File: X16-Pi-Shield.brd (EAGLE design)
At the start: 80.2 x 73 mm, 55 parts, among them J1 CONN_DF13-4P-1.25DSA, J2 CONN_DF13-4P-1.25DSA, J3 CONN_DF13-4P-1.25DSA, Q2 2.5A/30V/105mΩ, Q3 220mA/50V/3.5Ω, Q4 220mA/50V/3.5Ω, Q5 220mA/50V/3.5Ω, U2 MAX1136EUA-T, Y2 ECS-80-S-4X

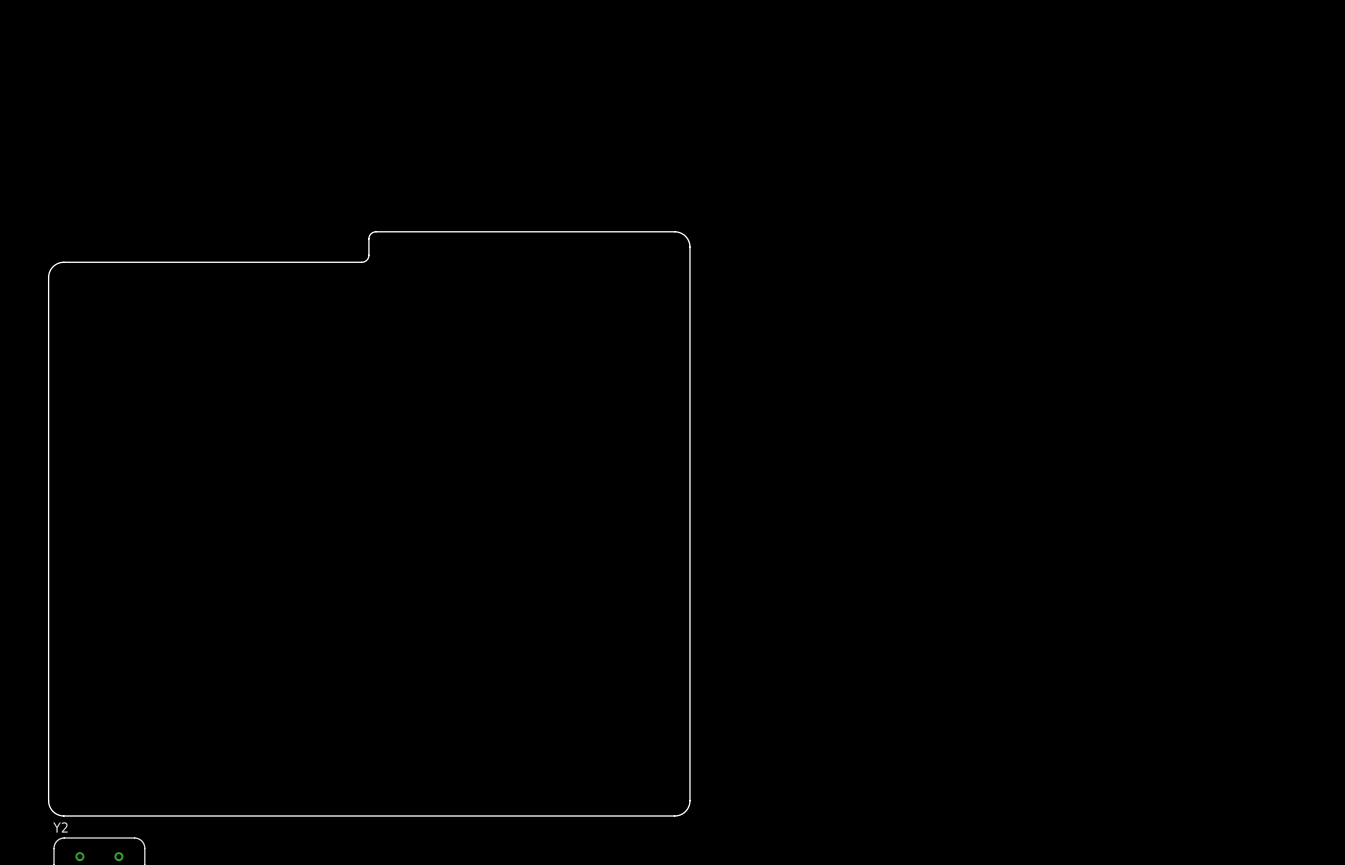
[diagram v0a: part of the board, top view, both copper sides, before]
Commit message: edited schematic for new connector
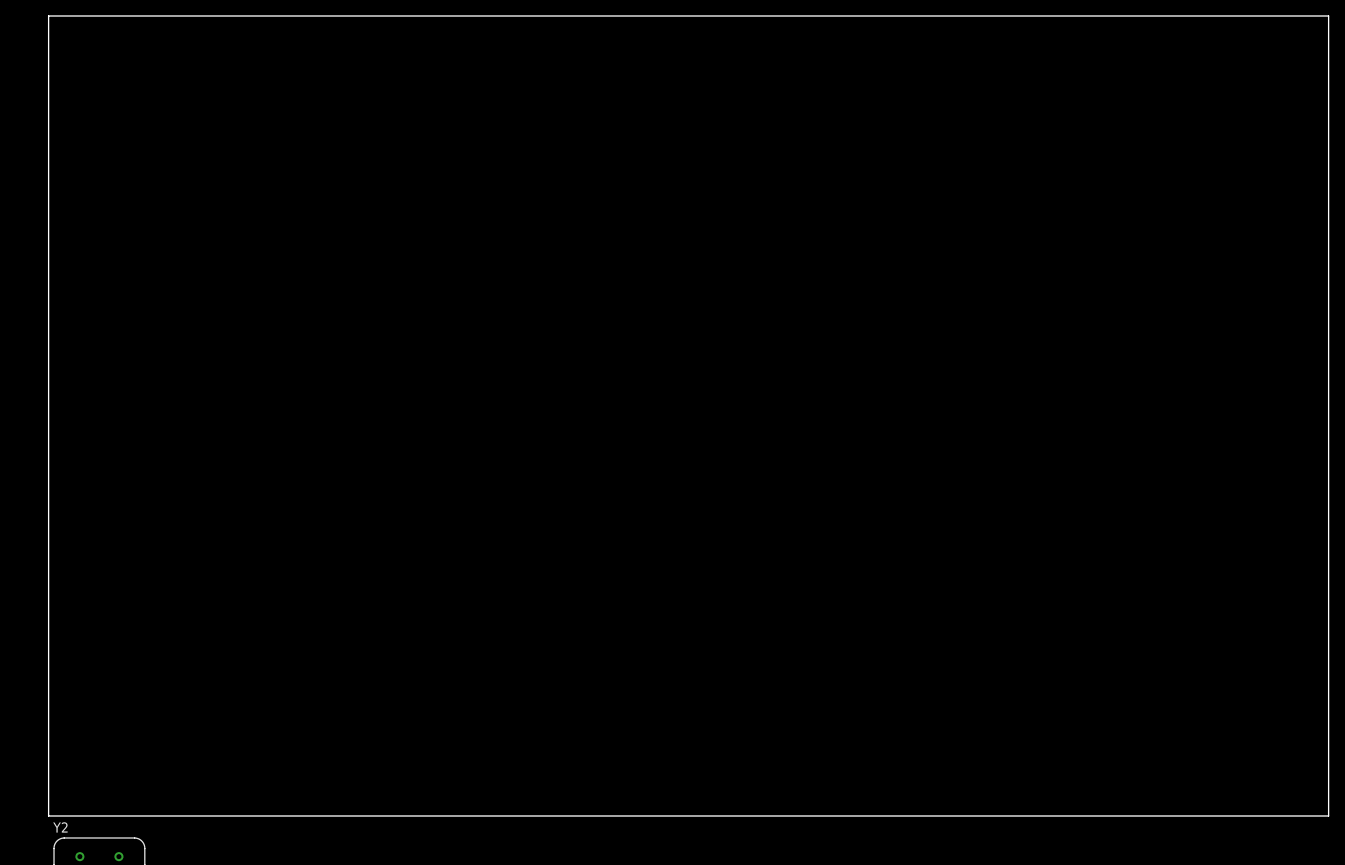
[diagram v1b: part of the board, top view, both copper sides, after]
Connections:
- net GPIO_6 renamed SA0
- removed net N$42: U$1.1
- new net CTRL: U$1.15
- new net DGND: U$1.31
- new net SA1: U$1.12
- new net SALERT: U$1.33
- net 3V3: now also U$1.1
- net GPIO_10: no longer U$1.31
- net GPIO_11: no longer U$1.15
- net GPIO_7: no longer U$1.12
- net GPIO_8: no longer U$1.32
- net GPIO_9: no longer U$1.33
- net SCL: now also U$1.32
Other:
- board size 80.2 x 73 mm -> 160 x 100 mm

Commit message: added connector
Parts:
- added J4: SAMTEC-HTST-110-04-X-D-RAJ, SAMTEC-HTST-110-04-X-D-RA:SAMTEC-HTST-110-04-X-D-RA
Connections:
- net 5V: now also J4.1
- net CLK: now also J4.18
- net CS: now also J4.20
- net CTRL: now also J4.7
- net DGND: now also J4.9
- net GND: now also J4.3
- net GPIO1: now also J4.2
- net GPIO2: now also J4.4
- net GPIO3: now also J4.6
- net GPIO4: now also J4.8
- net MISO: now also J4.14
- net MOSI: now also J4.16
- net SA0: now also J4.19
- net SA1: now also J4.17
- net SALERT: now also J4.13
- net SCL: now also J4.15
- net SDA: now also J4.11
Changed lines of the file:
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@@
 <attribute name="SPICEPREFIX" value="X" x="-24.13" y="-312.42" size="1.778" layer="27" display="off"/>
+</element>
+<element name="J4" library="SAMTEC-HTST-110-04-X-D-RA" package="SAMTEC-HTST-110-04-X-D-RA" value="SAMTEC-HTST-110-04-X-D-RAJ" x="-5.08" y="-325.12" smashed="yes">
+<attribute name="NAME" x="13.123" y="-316.266" size="1.905" layer="25"/>
+<attribute name="VALUE" x="-5.08" y="-319.216" size="0.635" layer="27" align="bottom-center"/>
 </element>
 </elements>
@@
 <contactref element="U$9" pad="6"/>
 <contactref element="U$9" pad="10"/>
+<contactref element="J4" pad="3"/>
 <wire x1="-22.01" y1="-234.95" x2="-18.2" y2="-234.95" width="0" layer="19" extent="1-1"/>
 <wire x1="-22.86" y1="-240.03" x2="-22.01" y2="-234.95" width="0" layer="19" extent="1-1"/>
@@
 <wire x1="-11.938" y1="-311.15" x2="-11.85" y2="-294.64" width="0" layer="19" extent="1-1"/>
 <wire x1="-17.018" y1="-311.15" x2="-11.938" y2="-311.15" width="0" layer="19" extent="1-1"/>
+<wire x1="3.81" y1="-317.246" x2="-11.938" y2="-311.15" width="0" layer="19" extent="1-1"/>
 <wire x1="-22.01" y1="-182.88" x2="-24.13" y2="-204.47" width="0" layer="19" extent="1-1"/>
 <wire x1="-12.065" y1="-177.8" x2="-22.01" y2="-182.88" width="0" layer="19" extent="1-1"/>
@@
 <contactref element="U$1" pad="24"/>
 <contactref element="J12" pad="5"/>
+<contactref element="J4" pad="20"/>
 <wire x1="21.0566" y1="-19.8882" x2="-12.7" y2="-96.52" width="0" layer="19" extent="1-1"/>
+<wire x1="-16.51" y1="-319.786" x2="-12.7" y2="-96.52" width="0" layer="19" extent="1-1"/>
 </signal>
 <signal name="A_INT">
@@
 <contactref element="U$1" pad="23"/>
 <contactref element="J12" pad="2"/>
+<contactref element="J4" pad="18"/>
 <wire x1="21.0566" y1="-22.4282" x2="-20.32" y2="-96.52" width="0" layer="19" extent="1-1"/>
+<wire x1="-13.97" y1="-319.786" x2="-20.32" y2="-96.52" width="0" layer="19" extent="1-1"/>
 </signal>
 <signal name="MISO">
 <contactref element="U$1" pad="21"/>
 <contactref element="J12" pad="4"/>
+<contactref element="J4" pad="14"/>
 <wire x1="18.5166" y1="-22.4282" x2="-15.24" y2="-96.52" width="0" layer="19" extent="1-1"/>
+<wire x1="-8.89" y1="-319.786" x2="-15.24" y2="-96.52" width="0" layer="19" extent="1-1"/>
 </signal>
 <signal name="MOSI">
 <contactref element="U$1" pad="19"/>
 <contactref element="J12" pad="3"/>
+<contactref element="J4" pad="16"/>
 <wire x1="15.9766" y1="-22.4282" x2="-17.78" y2="-96.52" width="0" layer="19" extent="1-1"/>
+<wire x1="-11.43" y1="-319.786" x2="-17.78" y2="-96.52" width="0" layer="19" extent="1-1"/>
 </signal>
 <signal name="N$34">
@@
 <contactref element="J3" pad="3"/>
 <contactref element="J2" pad="3"/>
+<contactref element="J4" pad="11"/>
 <wire x1="-17.78" y1="-116.84" x2="-9.525" y2="-177.8" width="0" layer="19" extent="1-1"/>
 <wire x1="-23.71" y1="-107.95" x2="-17.78" y2="-116.84" width="0" layer="19" extent="1-1"/>
@@
 <wire x1="-15.56" y1="-289.29" x2="-9.525" y2="-177.8" width="0" layer="19" extent="1-1"/>
 <wire x1="-14.39" y1="-299.72" x2="-15.56" y2="-289.29" width="0" layer="19" extent="1-1"/>
+<wire x1="-6.35" y1="-317.246" x2="-14.39" y2="-299.72" width="0" layer="19" extent="1-1"/>
 </signal>
 <signal name="3V3">
@@
 <contactref element="R24" pad="2"/>
 <contactref element="U$1" pad="32"/>
+<contactref element="J4" pad="15"/>
 <wire x1="-20.32" y1="-116.84" x2="-6.985" y2="-177.8" width="0" layer="19" extent="1-1"/>
 <wire x1="-23.71" y1="-111.76" x2="-20.32" y2="-116.84" width="0" layer="19" extent="1-1"/>
@@
 <wire x1="-20.64" y1="-289.29" x2="-6.985" y2="-177.8" width="0" layer="19" extent="1-1"/>
 <wire x1="-18.2" y1="-299.72" x2="-20.64" y2="-289.29" width="0" layer="19" extent="1-1"/>
+<wire x1="-11.43" y1="-317.246" x2="-18.2" y2="-299.72" width="0" layer="19" extent="1-1"/>
 </signal>
 <signal name="PI_POWER">
@@
 <contactref element="C13" pad="1"/>
 <contactref element="U$9" pad="8"/>
+<contactref element="J4" pad="1"/>
 <wire x1="-23.65" y1="-227.965" x2="-23.65" y2="-229.235" width="0" layer="19" extent="1-1"/>
 <wire x1="-23.65" y1="-226.695" x2="-23.65" y2="-227.965" width="0" layer="19" extent="1-1"/>
@@
 <wire x1="-22.01" y1="-303.53" x2="-22.01" y2="-299.72" width="0" layer="19" extent="1-1"/>
 <wire x1="-14.478" y1="-311.15" x2="-22.01" y2="-303.53" width="0" layer="19" extent="1-1"/>
+<wire x1="6.35" y1="-317.246" x2="-14.478" y2="-311.15" width="0" layer="19" extent="1-1"/>
 </signal>
 <signal name="IMU_RESET1">
@@
 <signal name="GPIO1">
 <contactref element="U$9" pad="1"/>
+<contactref element="J4" pad="2"/>
+<wire x1="6.35" y1="-319.786" x2="-22.098" y2="-308.61" width="0" layer="19" extent="1-1"/>
 </signal>
 <signal name="GPIO2">
 <contactref element="U$9" pad="3"/>
+<contactref element="J4" pad="4"/>
+<wire x1="3.81" y1="-319.786" x2="-19.558" y2="-308.61" width="0" layer="19" extent="1-1"/>
 </signal>
 <signal name="GPIO3">
 <contactref element="U$9" pad="5"/>
+<contactref element="J4" pad="6"/>
+<wire x1="1.27" y1="-319.786" x2="-17.018" y2="-308.61" width="0" layer="19" extent="1-1"/>
 </signal>
 <signal name="GPIO4">
 <contactref element="U$9" pad="7"/>
+<contactref element="J4" pad="8"/>
+<wire x1="-1.27" y1="-319.786" x2="-14.478" y2="-308.61" width="0" layer="19" extent="1-1"/>
 </signal>
 <signal name="GPIO5">
@@
 <signal name="CTRL">
 <contactref element="U$1" pad="15"/>
+<contactref element="J4" pad="7"/>
+<wire x1="10.8966" y1="-22.4282" x2="-1.27" y2="-317.246" width="0" layer="19" extent="1-1"/>
 </signal>
 <signal name="DGND">
 <contactref element="U$1" pad="31"/>
+<contactref element="J4" pad="9"/>
+<wire x1="31.2166" y1="-22.4282" x2="-3.81" y2="-317.246" width="0" layer="19" extent="1-1"/>
 </signal>
 <signal name="SALERT">
 <contactref element="U$1" pad="33"/>
+<contactref element="J4" pad="13"/>
+<wire x1="33.7566" y1="-22.4282" x2="-8.89" y2="-317.246" width="0" layer="19" extent="1-1"/>
 </signal>
 <signal name="SA1">
 <contactref element="U$1" pad="12"/>
+<contactref element="J4" pad="17"/>
+<wire x1="5.8166" y1="-19.8882" x2="-13.97" y2="-317.246" width="0" layer="19" extent="1-1"/>
 </signal>
 <signal name="SA0">
 <contactref element="U$1" pad="40"/>
+<contactref element="J4" pad="19"/>
+<wire x1="41.3766" y1="-19.8882" x2="-16.51" y2="-317.246" width="0" layer="19" extent="1-1"/>
 </signal>
 </signals>

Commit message: added some nets
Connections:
- removed net N$34: U$1.17
- net 3V3: now also U$1.17
- net GPIO5: now also J4.10
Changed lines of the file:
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@@
 <wire x1="-11.43" y1="-319.786" x2="-17.78" y2="-96.52" width="0" layer="19" extent="1-1"/>
-</signal>
-<signal name="N$34">
-<contactref element="U$1" pad="17"/>
 </signal>
 <signal name="GPIO_11">
@@
 <contactref element="U$9" pad="12"/>
 <contactref element="U$1" pad="1"/>
+<contactref element="U$1" pad="17"/>
 <wire x1="-24.13" y1="-199.39" x2="-18.2" y2="-212.09" width="0" layer="19" extent="1-1"/>
 <wire x1="-19.4564" y1="-196.85" x2="-24.13" y2="-199.39" width="0" layer="19" extent="1-1"/>
@@
 <wire x1="-19.715" y1="-71.12" x2="-19.715" y2="-80.01" width="0" layer="19" extent="1-1"/>
 <wire x1="-6.87" y1="-22.43" x2="-19.715" y2="-71.12" width="0" layer="19" extent="1-1"/>
+<wire x1="13.4366" y1="-22.4282" x2="-6.87" y2="-22.43" width="0" layer="19" extent="1-1"/>
 </signal>
 <signal name="SCL">
@@
 <signal name="GPIO5">
 <contactref element="U$9" pad="9"/>
+<contactref element="J4" pad="10"/>
+<wire x1="-11.938" y1="-308.61" x2="-3.81" y2="-319.786" width="0" layer="19" extent="1-1"/>
 </signal>
 <signal name="GPIO6">

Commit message: fixed library problems
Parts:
- removed C7: 4.7uF, SparkFun-Capacitors:0603
- removed JP5: JUMPER-SMT_2_NO_SILK, SparkFun-Jumpers:SMT-JUMPER_2_NO_SILK
- removed U$3: ADAFRUIT-FXOS8700-FXAS21002, X15-Pi-Shield-Parts:ADAFRUIT-FXOS8700-FXAS21002
- removed U$5: ADAFRUIT-BNO055, X15-Pi-Shield-Parts:ADAFRUIT-BNO055
- removed U$9: 8X_CONN, X15-Pi-Shield-Parts:IPL7X2
- added C3: 4.7uF, SparkFun-Capacitors:0603
- added JP7: JUMPER-SMT_2_NO_SILK, SparkFun-Jumpers:SMT-JUMPER_2_NO_SILK
- added U$2: CONN_ADAFRUIT-BNO055, X16-Pi-Shield:ADAFRUIT-BNO055
- added U$4: CONN_ADAFRUIT-FXOS8700-FXAS21002, X16-Pi-Shield:ADAFRUIT-FXOS8700-FXAS21002
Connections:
- removed net 3VO_2: U$5.3VO
- removed net A_INT1: U$3.AI1
- removed net GPIO6: U$9.11
- removed net GPIO_10: U$9.14
- removed net GPIO_11: U$9.4
- removed net GPIO_7: U$9.13
- removed net GPIO_8: U$9.15
- removed net GPIO_9: U$9.16
- removed net IMU_INT1: U$3.GI1
- removed net IMU_RESET1: U$3.RST
- removed net N$8: JP5.2, U$5.ADR
- removed net SCL1: U$3.SCL
- removed net SDA1: U$3.SDA
- new net 3V0_2: U$2.3VO
- new net N$17: JP7.2, U$2.ADR
- net 3V3: now also C3.1, JP7.1, U$2.VIN, U$4.VIN; no longer C7.1, JP5.1, U$3.VIN, U$5.VIN, U$9.12
- net 3VO_1: now also U$4.3VO; no longer U$3.3VO
- net 5V: no longer U$9.8
- net A_INT: now also U$4.AI1
- net GND: now also C3.2, U$2.GND, U$4.GND; no longer C7.2, U$3.GND, U$5.GND, U$9.10, U$9.6
- net GPIO1: no longer U$9.1
- net GPIO2: no longer U$9.3
- net GPIO3: no longer U$9.5
- net GPIO4: no longer U$9.7
- net GPIO5: no longer U$9.9
- net IMU_INT: now also U$2.INT, U$4.GI1; no longer U$5.INT
- net IMU_RESET: now also U$2.RST, U$4.RST; no longer U$5.RST
- net SCL: now also U$2.SCL, U$4.SCL; no longer U$5.SCL
- net SDA: now also U$2.SDA, U$4.SDA; no longer U$5.SDA

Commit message: made some changes
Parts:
- U$7: device X15-Pi-Shield-Parts:DISCRETECOMPONENTS_SW_2512 -> X16-Pi-Shield:DISCRETECOMPONENTS_SW_2512
- U$8: value MCR1101 -> IC_MCR1101; device X15-Pi-Shield-Parts:SOIC-16 -> X16-Pi-Shield:SOIC-16
- U2: device X15-Pi-Shield-Parts:21-0036K -> X16-Pi-Shield:21-0036K
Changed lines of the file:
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@@
 <attribute name="VALUE" x="-19.05" y="-212.852" size="0.6096" layer="27" font="vector" ratio="20" align="top-center"/>
 </element>
-<element name="U$8" library="X15-Pi-Shield-Parts" package="SOIC-16" value="MCR1101" x="-19.05" y="-224.79" smashed="yes">
+<element name="U$8" library="X16-Pi-Shield" package="SOIC-16" value="IC_MCR1101" x="-19.05" y="-224.79" smashed="yes">
 <attribute name="NAME" x="-23.55" y="-218.39" size="0.8128" layer="25"/>
 <attribute name="VALUE" x="-23.45" y="-231.89" size="0.8128" layer="27"/>
@@
 <attribute name="VALUE" x="-19.939" y="-246.38" size="0.6096" layer="27" font="vector" ratio="20" rot="R90" align="top-center"/>
 </element>
-<element name="U$7" library="X15-Pi-Shield-Parts" package="DISCRETECOMPONENTS_SW_2512" value="" x="-20.32" y="-254" smashed="yes">
+<element name="U$7" library="X16-Pi-Shield" package="DISCRETECOMPONENTS_SW_2512" package3d_urn="urn:adsk.eagle:package:24384574/2" value="" x="-20.32" y="-254" smashed="yes">
 <attribute name="NAME" x="-20.32" y="-252.095" size="1.27" layer="25" align="bottom-center"/>
 <attribute name="VALUE" x="-20.32" y="-255.905" size="1.27" layer="27" align="top-center"/>
@@
 <attribute name="VALUE" x="-24.13" y="-283.972" size="0.6096" layer="27" font="vector" ratio="20"/>
 </element>
-<element name="U2" library="X15-Pi-Shield-Parts" package="21-0036K" value="MAX1136EUA-T" x="-21.59" y="-294.64" smashed="yes">
+<element name="U2" library="X16-Pi-Shield" package="21-0036K" value="MAX1136EUA-T" x="-21.59" y="-294.64" smashed="yes">
 <attribute name="DESCRIPTION" value=" 2.7V to 3.6V and 4.5V to 5.5V, Low-Power, 4-/12-Channel, 2-Wire Serial 10-Bit AD " x="-21.59" y="-287.02" size="1.778" layer="27" display="off"/>
 <attribute name="DIGI-KEY_PART_NUMBER" value="MAX1136EUA+-ND" x="-21.59" y="-287.02" size="1.778" layer="27" display="off"/>
@@
 </board>
 </drawing>
+<compatibility>
+<note version="8.3" severity="warning">
+Since Version 8.3, EAGLE supports URNs for individual library
+assets (packages, symbols, and devices). The URNs of those assets
+will not be understood (or retained) with this version.
+</note>
+<note version="8.3" severity="warning">
+Since Version 8.3, EAGLE supports the association of 3D packages
+with devices in libraries, schematics, and board files. Those 3D
+packages will not be understood (or retained) with this version.
+</note>
+</compatibility>
 </eagle>

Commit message: updated schematic and library
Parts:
- removed C10, C12, C13: 0.1uF, SparkFun-Capacitors:0603
- removed C11: 10nF, SparkFun-Capacitors:0603
- removed Q4, Q5: 220mA/50V/3.5Ω, SparkFun-DiscreteSemi:SOT23-3
- removed R23, R24, R25, R26: 10k, SparkFun-Resistors:0603
- removed U$8: IC_MCR1101, X16-Pi-Shield:SOIC-16
- added C4: 10uF, SparkFun-Capacitors:0603
- added C5: 22uF, SparkFun-Capacitors:0603
- added U1: INA260AIPW, X16-Pi-Shield:SOP65P640X120-16N
- U2: value MAX1136EUA-T -> AZ1117IH-3.3TRG1; device X16-Pi-Shield:21-0036K -> X16-Pi-Shield:SOT230P700X185-4N
- moved U2 86.7 mm to (-38.1, -379.7)
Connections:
- removed net AMP_OUT: U$8.12, U2.2
- removed net GPIO5: J4.10
- removed net GPIO_5: U$1.38
- removed net N$11: C11.1, U$8.13
- removed net POWER: U$1.2, U$1.4
- removed net SCL_ADC: Q4.3, R23.1, U2.5
- removed net SDA_ADC: Q5.3, R26.1, U2.6
- new net 5V_EXT: C4.2, J4.1, U1.1, U1.12, U1.2, U1.3, U2.3
- new net ALERT: U$1.38, U1.7
- new net VS: C5.2, U1.10, U2.2
- net !AMP_FAULT: no longer U$8.9
- net 3V3: no longer Q4.1, Q5.1, R24.1, R25.1
- net 5V: now also U$1.2, U$1.4, U1.14, U1.15, U1.16; no longer C10.1, C12.1, C13.1, J4.1, R23.2, R26.2, U$8.10, U$8.5, U$8.6, U$8.7, U$8.8, U2.4, U2.8
- net 5V_RAW: no longer U$8.1, U$8.2, U$8.3, U$8.4
- net AIN2: no longer U2.3
- net GND: now also C4.1, C5.1, U1.11, U1.6, U2.1; no longer C10.2, C11.2, C12.2, C13.2, U$8.11, U$8.14, U$8.15, U2.7
- net OCD: no longer U$8.16
- net SA0: now also U1.5
- net SA1: now also U1.4
- net SCL: now also U1.9; no longer Q4.2, R24.2
- net SDA: now also U1.8; no longer Q5.2, R25.2

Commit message: final schematic
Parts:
- added JP5, JP8: JUMPER-SMT_2_NO_SILK, SparkFun-Jumpers:SMT-JUMPER_2_NO_SILK
- added TP4, TP5: TEST-POINT3, SparkFun-Connectors:PAD.03X.03
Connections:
- new net N$3: JP8.1, U1.5
- net SA0: now also TP4.1; no longer U1.5
- net SA1: now also JP5.1, TP5.1
- net VS: now also JP5.2, JP8.2, U2.4
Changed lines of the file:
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@@
 <attribute name="VALUE" x="-40.64" y="-393.192" size="0.6096" layer="27" font="vector" ratio="20" align="top-center"/>
+</element>
+<element name="TP4" library="SparkFun-Connectors" package="PAD.03X.03" value="TEST-POINT3" x="-41.91" y="-396.24" smashed="yes"/>
+<element name="TP5" library="SparkFun-Connectors" package="PAD.03X.03" value="TEST-POINT3" x="-41.91" y="-398.78" smashed="yes"/>
+<element name="JP5" library="SparkFun-Jumpers" package="SMT-JUMPER_2_NO_SILK" value="JUMPER-SMT_2_NO_SILK" x="-36.83" y="-402.59" smashed="yes">
+<attribute name="NAME" x="-36.83" y="-401.447" size="0.6096" layer="25" font="vector" ratio="20" align="bottom-center"/>
+<attribute name="VALUE" x="-36.83" y="-403.733" size="0.6096" layer="27" font="vector" ratio="20" align="top-center"/>
+</element>
+<element name="JP8" library="SparkFun-Jumpers" package="SMT-JUMPER_2_NO_SILK" value="JUMPER-SMT_2_NO_SILK" x="-36.83" y="-407.67" smashed="yes">
+<attribute name="NAME" x="-36.83" y="-406.527" size="0.6096" layer="25" font="vector" ratio="20" align="bottom-center"/>
+<attribute name="VALUE" x="-36.83" y="-408.813" size="0.6096" layer="27" font="vector" ratio="20" align="top-center"/>
 </element>
 </elements>
@@
 <contactref element="J4" pad="17"/>
 <contactref element="U1" pad="4"/>
+<contactref element="TP5" pad="1"/>
+<contactref element="JP5" pad="1"/>
+<wire x1="-37.2364" y1="-402.59" x2="-41.91" y2="-398.78" width="0" layer="19" extent="1-1"/>
+<wire x1="-32.08" y1="-380.675" x2="-41.91" y2="-398.78" width="0" layer="19" extent="1-1"/>
 <wire x1="-13.97" y1="-317.246" x2="-32.08" y2="-380.675" width="0" layer="19" extent="1-1"/>
 <wire x1="5.8166" y1="-19.8882" x2="-13.97" y2="-317.246" width="0" layer="19" extent="1-1"/>
@@
 <contactref element="U$1" pad="40"/>
 <contactref element="J4" pad="19"/>
-<contactref element="U1" pad="5"/>
-<wire x1="-16.51" y1="-317.246" x2="-32.08" y2="-381.325" width="0" layer="19" extent="1-1"/>
+<contactref element="TP4" pad="1"/>
+<wire x1="-16.51" y1="-317.246" x2="-41.91" y2="-396.24" width="0" layer="19" extent="1-1"/>
 <wire x1="41.3766" y1="-19.8882" x2="-16.51" y2="-317.246" width="0" layer="19" extent="1-1"/>
 </signal>
@@
 <contactref element="U2" pad="2"/>
 <contactref element="C5" pad="2"/>
+<contactref element="U2" pad="4"/>
+<contactref element="JP5" pad="2"/>
+<contactref element="JP8" pad="2"/>
+<wire x1="-36.4236" y1="-402.59" x2="-36.4236" y2="-407.67" width="0" layer="19" extent="1-1"/>
+<wire x1="-39.79" y1="-392.43" x2="-36.4236" y2="-402.59" width="0" layer="19" extent="1-1"/>
 <wire x1="-41.2" y1="-379.73" x2="-39.79" y2="-392.43" width="0" layer="19" extent="1-1"/>
-<wire x1="-26.34" y1="-382.625" x2="-41.2" y2="-379.73" width="0" layer="19" extent="1-1"/>
+<wire x1="-35" y1="-379.73" x2="-41.2" y2="-379.73" width="0" layer="19" extent="1-1"/>
+<wire x1="-26.34" y1="-382.625" x2="-35" y2="-379.73" width="0" layer="19" extent="1-1"/>
+</signal>
+<signal name="N$3">
+<contactref element="U1" pad="5"/>
+<contactref element="JP8" pad="1"/>
+<wire x1="-32.08" y1="-381.325" x2="-37.2364" y2="-407.67" width="0" layer="19" extent="1-1"/>
 </signal>
 </signals>
